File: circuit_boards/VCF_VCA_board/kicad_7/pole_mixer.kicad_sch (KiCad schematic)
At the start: 20 parts, among them U4 TL072

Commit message: Progress on circuit boards
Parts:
- C504: value ? -> 100p
- R509: value ? -> 56k
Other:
- note added: "Highpass and Bandpass responses are generated by "pole mixing"; weighted amounts of the various filter outputs and dry signal. Extra do-not-place resistors are left in place for experimentation with other modes."
- note removed: "Highpass and Bandpass responses are generated by "pole mixing"; weighted amounts of the various filter outputs and dry signal. Extra do-not-place resistors are left in place for experimentation or other modes."
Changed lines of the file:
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@@
   (title_block
     (title "MICRO-OX VCF/VCA board")
-    (date "2023-03-21")
+    (date "2023-04-13")
     (rev "0")
     (comment 1 "creativecommons.org/licenses/by/4.0/")
@@
     (stroke (width 0) (type default))
   )
-  (text "Highpass and Bandpass responses\nare generated by \"pole mixing\";\nweighted amounts of the various\nfilter outputs and dry signal.\n\nExtra do-not-place resistors are\nleft in place for experimentation\nor other modes."
+  (text "Highpass and Bandpass responses\nare generated by \"pole mixing\";\nweighted amounts of the various\nfilter outputs and dry signal.\n\nExtra do-not-place resistors are\nleft in place for experimentation\nwith other modes."
     (at 105.41 191.77 0)
     (effects (font (size 2.5 2.5) (thickness 0.35) bold) (justify left bottom))
@@
       (effects (font (size 1.27 1.27)))
     )
-    (property "Value" "?" (at 146.05 124.46 90)
+    (property "Value" "56k" (at 146.05 124.46 90)
       (effects (font (size 1.27 1.27)))
     )
@@
       (effects (font (size 1.27 1.27)))
     )
-    (property "Value" "?" (at 146.05 54.61 90)
+    (property "Value" "56k" (at 146.05 54.61 90)
       (effects (font (size 1.27 1.27)))
     )
@@
       (effects (font (size 1.27 1.27)))
     )
-    (property "Value" "?" (at 146.05 41.91 90)
+    (property "Value" "100p" (at 146.05 41.91 90)
       (effects (font (size 1.27 1.27)))
     )
@@
       (effects (font (size 1.27 1.27)))
     )
-    (property "Value" "?" (at 146.05 111.76 90)
-      (effects (font (size 1.27 1.27)))
-    )
+    (property "Value" "100p" (at 146.05 111.76 90)
+      (effects (font (size 1.27 1.27)))
+    )

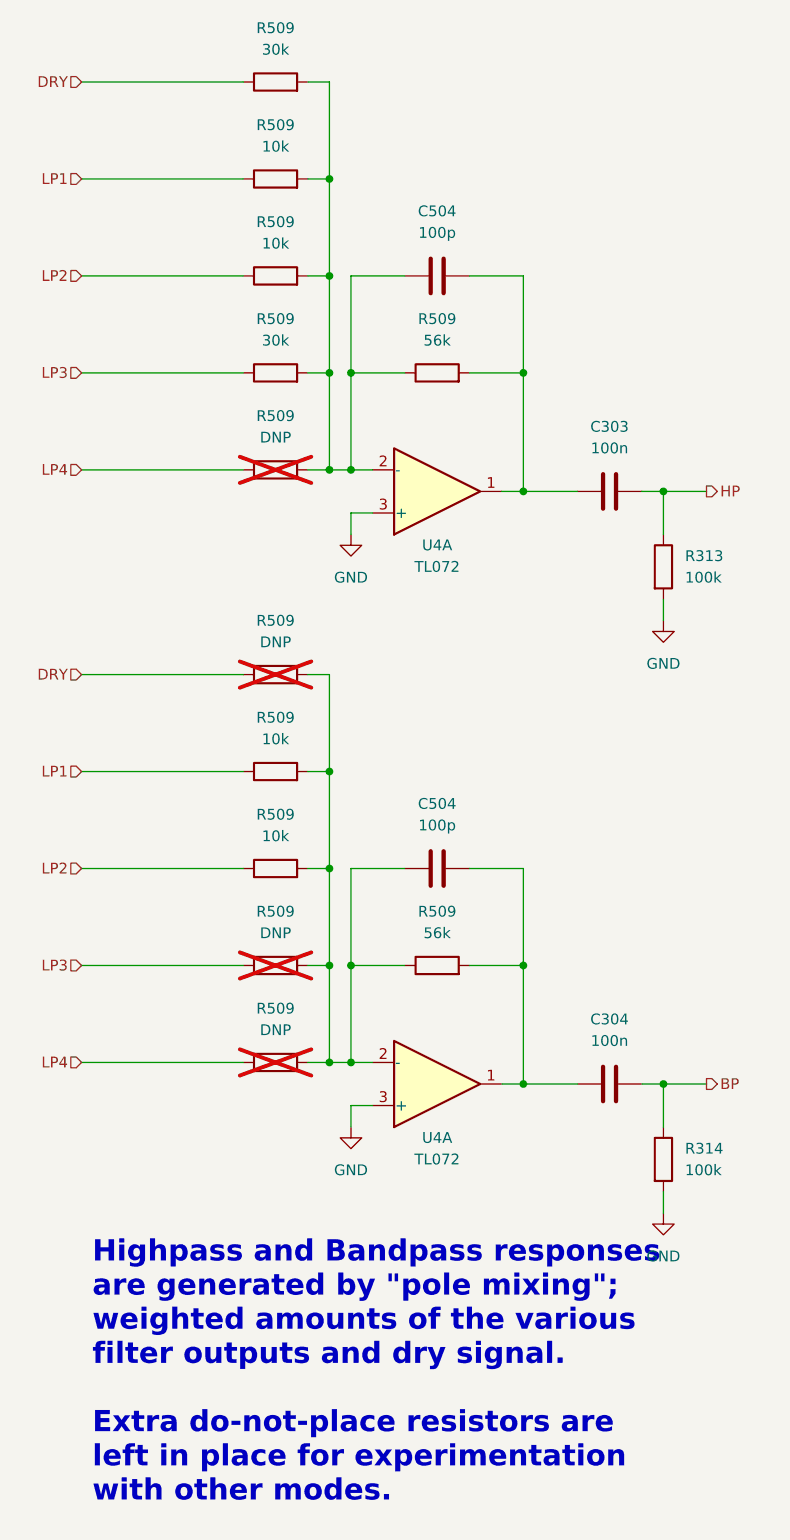
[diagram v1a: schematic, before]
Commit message: Update PCBs, tweak vals, add VCF CV from DAC
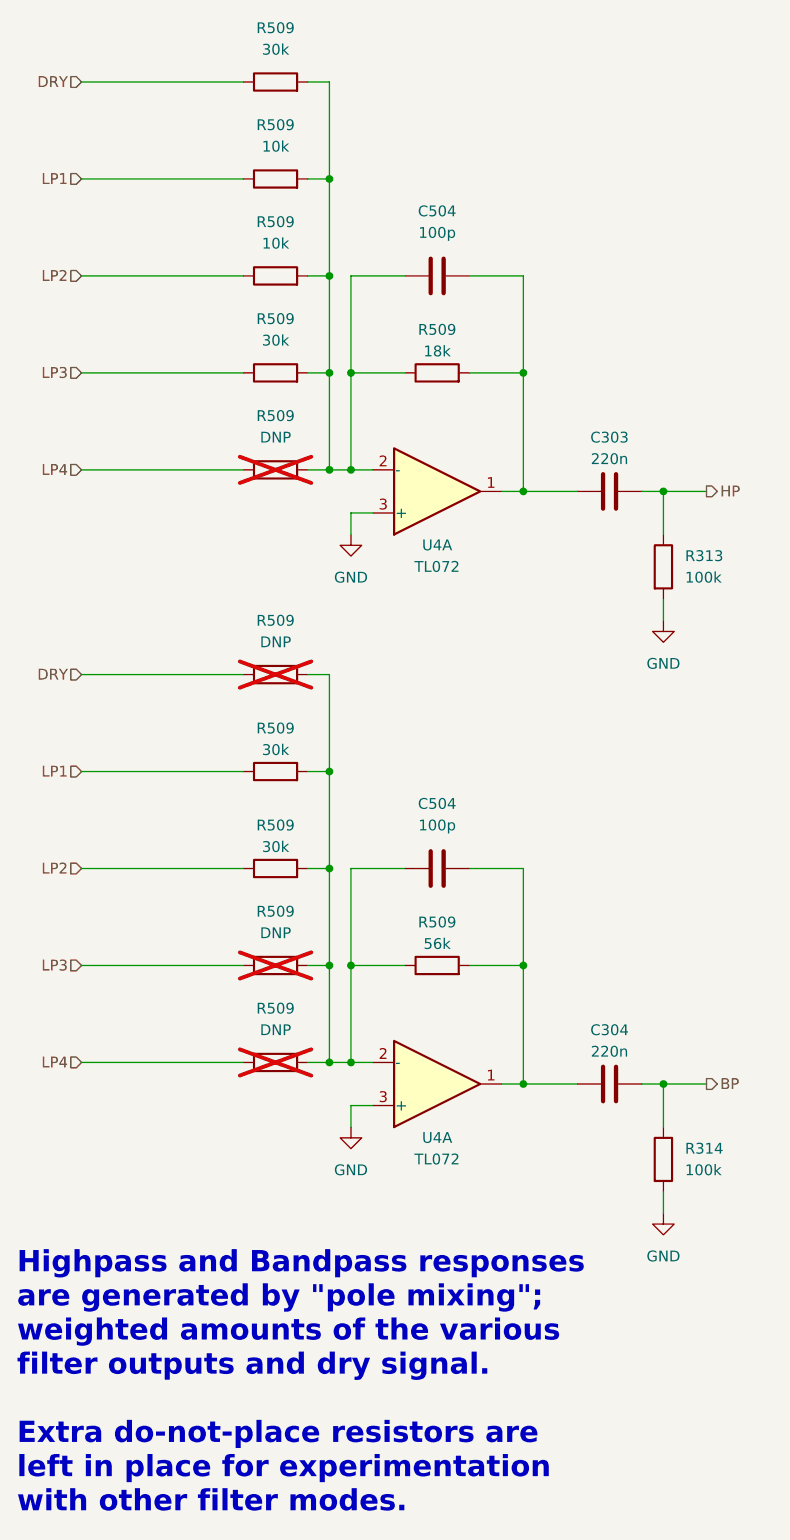
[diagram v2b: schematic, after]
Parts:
- C303, C304: value 100n -> 220n
- R509: value 56k -> 18k
- R509: value 10k -> 30k
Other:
- note added: "Highpass and Bandpass responses are generated by "pole mixing"; weighted amounts of the various filter outputs and dry signal. Extra do-not-place resistors are left in place for experimentation with other filter modes."
- note removed: "Highpass and Bandpass responses are generated by "pole mixing"; weighted amounts of the various filter outputs and dry signal. Extra do-not-place resistors are left in place for experimentation with other modes."
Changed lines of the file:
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@@
   (title_block
     (title "MICRO-OX VCF/VCA board")
-    (date "2023-04-13")
-    (rev "0")
+    (date "2023-04-25")
+    (rev "0.1")
     (comment 1 "creativecommons.org/licenses/by/4.0/")
     (comment 2 "License: CC by 4.0")
@@
     (stroke (width 0) (type default))
   )
-  (text "Highpass and Bandpass responses\nare generated by \"pole mixing\";\nweighted amounts of the various\nfilter outputs and dry signal.\n\nExtra do-not-place resistors are\nleft in place for experimentation\nwith other modes."
-    (at 105.41 191.77 0)
+  (text "Highpass and Bandpass responses\nare generated by \"pole mixing\";\nweighted amounts of the various\nfilter outputs and dry signal.\n\nExtra do-not-place resistors are\nleft in place for experimentation\nwith other filter modes."
+    (at 96.52 193.04 0)
     (effects (font (size 2.5 2.5) (thickness 0.35) bold) (justify left bottom))
   )
@@
   (symbol (lib_id "Device:C") (at 166.37 142.24 90) (unit 1)
     (in_bom yes) (on_board yes) (dnp no) (fields_autoplaced)
-    (property "Reference" "C304" (at 166.37 134.62 90)
-      (effects (font (size 1.27 1.27)))
-    )
-    (property "Value" "100n" (at 166.37 137.16 90)
+    (property "Reference" "C304" (at 166.37 135.89 90)
+      (effects (font (size 1.27 1.27)))
+    )
+    (property "Value" "220n" (at 166.37 138.43 90)
       (effects (font (size 1.27 1.27)))
     )
@@
   (symbol (lib_id "Device:R") (at 146.05 128.27 90) (unit 1)
     (in_bom yes) (on_board yes) (dnp no) (fields_autoplaced)
-    (property "Reference" "R509" (at 146.05 121.92 90)
-      (effects (font (size 1.27 1.27)))
-    )
-    (property "Value" "56k" (at 146.05 124.46 90)
+    (property "Reference" "R509" (at 146.05 123.19 90)
+      (effects (font (size 1.27 1.27)))
+    )
+    (property "Value" "56k" (at 146.05 125.73 90)
       (effects (font (size 1.27 1.27)))
     )
@@
   (symbol (lib_id "Device:R") (at 146.05 58.42 90) (unit 1)
     (in_bom yes) (on_board yes) (dnp no) (fields_autoplaced)
-    (property "Reference" "R509" (at 146.05 52.07 90)
-      (effects (font (size 1.27 1.27)))
-    )
-    (property "Value" "56k" (at 146.05 54.61 90)
+    (property "Reference" "R509" (at 146.05 53.34 90)
+      (effects (font (size 1.27 1.27)))
+    )
+    (property "Value" "18k" (at 146.05 55.88 90)
       (effects (font (size 1.27 1.27)))
     )
@@
   (symbol (lib_id "Device:R") (at 127 105.41 90) (unit 1)
     (in_bom yes) (on_board yes) (dnp no) (fields_autoplaced)
-    (property "Reference" "R509" (at 127 99.06 90)
-      (effects (font (size 1.27 1.27)))
-    )
-    (property "Value" "10k" (at 127 101.6 90)
+    (property "Reference" "R509" (at 127 100.33 90)
+      (effects (font (size 1.27 1.27)))
+    )
+    (property "Value" "30k" (at 127 102.87 90)
       (effects (font (size 1.27 1.27)))
     )
@@
   (symbol (lib_id "Device:C") (at 166.37 72.39 90) (unit 1)
     (in_bom yes) (on_board yes) (dnp no) (fields_autoplaced)
-    (property "Reference" "C303" (at 166.37 64.77 90)
-      (effects (font (size 1.27 1.27)))
-    )
-    (property "Value" "100n" (at 166.37 67.31 90)
+    (property "Reference" "C303" (at 166.37 66.04 90)
+      (effects (font (size 1.27 1.27)))
+    )
+    (property "Value" "220n" (at 166.37 68.58 90)
       (effects (font (size 1.27 1.27)))
     )
@@
   (symbol (lib_id "Device:R") (at 127 116.84 90) (unit 1)
     (in_bom yes) (on_board yes) (dnp no) (fields_autoplaced)
-    (property "Reference" "R509" (at 127 110.49 90)
-      (effects (font (size 1.27 1.27)))
-    )
-    (property "Value" "10k" (at 127 113.03 90)
-      (effects (font (size 1.27 1.27)))
-    )
+    (property "Reference" "R509" (at 127 111.76 90)
+      (effects (font (size 1.27 1.27)))
+    )
+    (property "Value" "30k" (at 127 114.3 90)
+      (effects (font (size 1.27 1.27)))
+    )

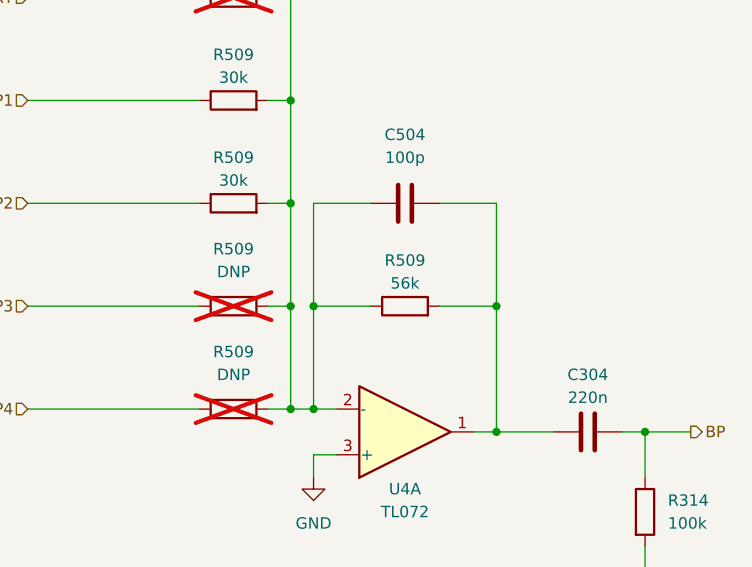
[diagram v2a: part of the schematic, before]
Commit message: Reduce bandpass gain
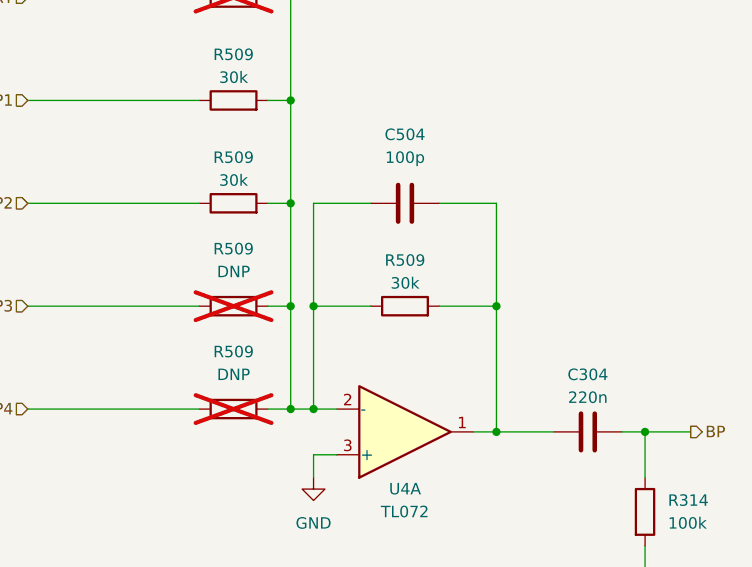
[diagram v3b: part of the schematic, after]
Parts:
- R509: value 56k -> 30k
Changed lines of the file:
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@@
       (effects (font (size 1.27 1.27)))
     )
-    (property "Value" "56k" (at 146.05 125.73 90)
+    (property "Value" "30k" (at 146.05 125.73 90)
       (effects (font (size 1.27 1.27)))
     )

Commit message: Turn down bandpass gain even more
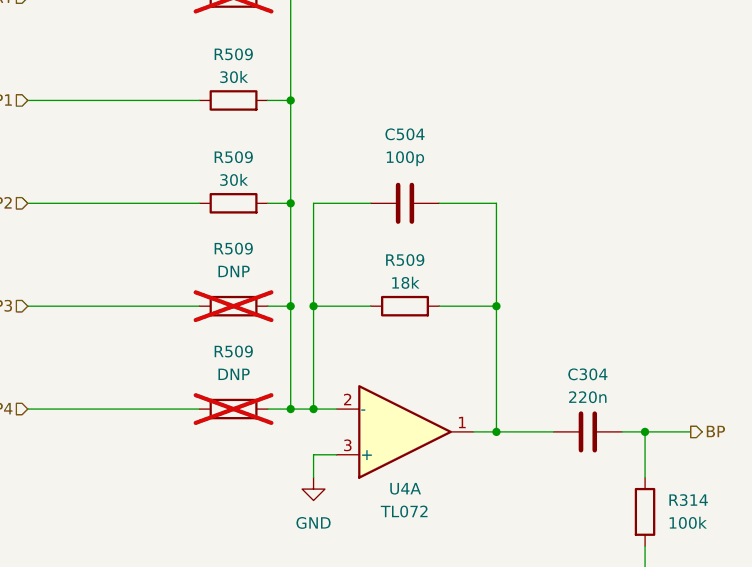
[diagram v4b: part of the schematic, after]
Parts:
- R509: value 30k -> 18k
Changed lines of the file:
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@@
       (effects (font (size 1.27 1.27)))
     )
-    (property "Value" "30k" (at 146.05 125.73 90)
+    (property "Value" "18k" (at 146.05 125.73 90)
       (effects (font (size 1.27 1.27)))
     )
